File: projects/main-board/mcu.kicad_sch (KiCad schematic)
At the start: 106 parts, among them J4 TC2030, J7 Conn_01x06, U1 STM32N657X0HxQ

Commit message: Updated schematics with new symbols
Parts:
- removed U1: STM32N657X0HxQ, VFBGA264, symbol stm32n_u:STM32N657X0HxQ
- added U15: STM32N657X0HxQ, footprint-library:STM32N645A0HxQ, symbol symbol-library:STM32N657X0HxQ
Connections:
- net 1V8: now also U15.G13 (VDD), U15.H12 (VDD), U15.H13 (VDD), U15.J12 (VDD), U15.J13 (VDD), U15.K13 (VDD)
- net BACKLIGHT_PWM: now also U15.B9 (PC6)
- net BOOT0: now also U15.G4 (BOOT0)
- net BUTTONS.B0: now also U15.R3 (PF0)
- net BUTTONS.B1: now also U15.P4 (PF1)
- net BUTTONS.B10: now also U15.L4 (PF10)
- net BUTTONS.B11: now also U15.P3 (PF11)
- net BUTTONS.B12: now also U15.T1 (PF12)
- net BUTTONS.B13: now also U15.R2 (PF13)
- net BUTTONS.B14: now also U15.N2 (PF14)
- net BUTTONS.B15: now also U15.N1 (PF15)
- net BUTTONS.B2: now also U15.N4 (PF2)
- net BUTTONS.B3: now also U15.M2 (PF3)
- net BUTTONS.B4: now also U15.L2 (PF4)
- net BUTTONS.B5: now also U15.M3 (PF5)
- net BUTTONS.B6: now also U15.L5 (PF6)
- net BUTTONS.B7: now also U15.M1 (PF7)
- net BUTTONS.B8: now also U15.N3 (PF8)
- net BUTTONS.B9: now also U15.P1 (PF9)
- net DEBUG_UART.RX: now also U15.R7 (PA10)
- net DEBUG_UART.TX: now also U15.P7 (PA9)
- net ESP32_EN: now also U15.F13 (PB3)
- net ESP32_GPIO.2: now also U15.C8 (PC12)
- net ESP32_GPIO.3: now also U15.A9 (PC1)
- net ESP32_GPIO.8: now also U15.F3 (PC13)
- net ESP32_GPIO.9: now also U15.A8 (PC10)
- net ESP32_UART.RX: now also U15.F17 (PE1)
- net ESP32_UART.TX: now also U15.F16 (PE0)
- net FLASH_OCTOSPI.RESET_N: now also U15.T16 (PN7)
- net GND: now also U15.A17 (VSS), U15.F10 (VSS), U15.F11 (VSS), U15.F12 (VSS), U15.F2 (VSSAPMU), U15.F7 (VSS), U15.G12 (VSS), U15.G6 (VSSAON), U15.H1 (VSSSMPS), U15.H2 (VSSSMPS), U15.H3 (VSSSMPS), U15.H4 (VSSSMPS), U15.H5 (VSSSMPS), U15.H6 (VSSSMPS), U15.K12 (VSS), U15.M10 (VSS), U15.M12 (VSS), U15.M13 (VSS), U15.M6 (VSSA), U15.M8 (VSS), U15.N11 (VSS), U15.N5 (VSS), U15.N7 (VSS), U15.N9 (VSS), U15.T2 (VREF-), U15.U1 (VSS), U15.U17 (VSS)
- net I2C1.SCL: now also U15.C11 (PE5)
- net I2C1.SDA: now also U15.D11 (PE6)
- net I2C4.SCL: now also U15.A11 (PE13)
- net I2C4.SDA: now also U15.B11 (PE14)
- net I2S.BCK: now also U15.E17 (PB6)
- net I2S.DACDAT: now also U15.E16 (PB7)
- net I2S.LRCK: now also U15.E15 (PB0)
- net I2S.MCLK: now also U15.F15 (PE2)
- net LCD.B0: now also U15.R6 (PG15)
- net LCD.B1: now also U15.R12 (PA7)
- net LCD.B2: now also U15.C16 (PB2)
- net LCD.B3: now also U15.L3 (PG6)
- net LCD.B4: now also U15.B1 (PH3)
- net LCD.B5: now also U15.B2 (PH6)
- net LCD.B6: now also U15.U8 (PA8)
- net LCD.B7: now also U15.T8 (PA2)
- net LCD.CLK: now also U15.C15 (PB13)
- net LCD.DE: now also U15.U9 (PG13)
- net LCD.EN: now also U15.D3 (PQ3)
- net LCD.G0: now also U15.T9 (PG12)
- net LCD.G1: now also U15.R9 (PG1)
- net LCD.G2: now also U15.P9 (PA1)
- net LCD.G3: now also U15.U10 (PA0)
- net LCD.G4: now also U15.D17 (PB15)
- net LCD.G5: now also U15.R10 (PB12)
- net LCD.G6: now also U15.P10 (PB11)
- net LCD.G7: now also U15.T14 (PG8)
- net LCD.HSYNC: now also U15.B17 (PB14)
- net LCD.R0: now also U15.R13 (PG0)
- net LCD.R1: now also U15.H14 (PD9)
- net LCD.R2: now also U15.B14 (PD15)
- net LCD.R3: now also U15.T12 (PB4(NJTRST))
- net LCD.R4: now also U15.F4 (PH4)
- net LCD.R5: now also U15.P12 (PA15(JTDI))
- net LCD.R6: now also U15.U13 (PG11)
- net LCD.R7: now also U15.E14 (PD8)
- net LCD.VSYNC: now also U15.E11 (PE11)
- net LEFT_MOTOR_PWM: now also U15.R8 (PA5)
- net NRST: now also U15.G3 (NRST)
- net PMIC_ALERT: now also U15.D13 (PD0)
- net PMIC_CHARGE_EN: now also U15.E13 (PD3)
- net PMIC_INPUT_VALID: now also U15.C12 (PD2)
- net PMIC_STATUS: now also U15.A14 (PD1)
- net RIGHT_MOTOR_PWM: now also U15.P8 (PA6)
- net SD.CLK: now also U15.D9 (PC2)
- net SD.CMD: now also U15.E10 (PC3)
- net SD.D0: now also U15.A10 (PC4)
- net SD.D1: now also U15.B10 (PC5)
- net SD.D2: now also U15.C10 (PC0)
- net SD.D3: now also U15.D10 (PE4)
- net SD.DETECT: now also U15.P14 (PN12)
- net SWCLK: now also U15.T6 (PA14(JTCK/SWCLK))
- net SWDIO: now also U15.U6 (PA13(JTMS/SWDIO))
- net USB.DM: now also U15.A5 (OTG1_HSDM)
- net USB.DP: now also U15.B5 (OTG1_HSDP)
- net USB_CC1: now also U15.A6 (UCPD1_CC1)
- net USB_CC2: now also U15.B6 (UCPD1_CC2)
- net V08CAP: now also U15.F1 (V08CAP)
- net VDDA18ADC: now also U15.N6 (VDDA18ADC)
- net VDDA18AON: now also U15.A1 (PDR_ON), U15.F6 (VDDA18AON)
- net VDDA18CSI: now also U15.R5 (VDDA18CSI)
- net VDDA18PLL: now also U15.M5 (VDDA18PLL)
- net VDDA18PMU: now also U15.G1 (VDDA18PMU)
- net VDDA18USB: now also U15.C5 (VDDA18USB)
- net VDDA33USB: now also U15.A4 (VDD33USB)
- net VDDCORE: now also U15.G2 (VFBSMPS), U15.L12 (VDDCORE), U15.L6 (VDDCORE), U15.M11 (VDDCORE), U15.M7 (VDDCORE), U15.M9 (VDDCORE), U15.N10 (VDDCORE), U15.N12 (VDDCORE), U15.N8 (VDDCORE), U15.P11 (VDDCORE)
- net VDDCSI: now also U15.R4 (VDDCSI)
- net VDDIO2: now also U15.L13 (VDDIO2), U15.L14 (VDDIO2), U15.M14 (VDDIO2), U15.M15 (VDDIO2)
- net VDDIO3: now also U15.N13 (VDDIO3), U15.P13 (VDDIO3)
- net VDDIO4: now also U15.E8 (VDDIO4), U15.F8 (VDDIO4)
- net VDDIO5: now also U15.E9 (VDDIO5), U15.F9 (VDDIO5)
- net VDDSMPS: now also U15.K1 (VDDSMPS), U15.K2 (VDDSMPS), U15.K3 (VDDSMPS), U15.K4 (VDDSMPS), U15.K5 (VDDSMPS), U15.K6 (VDDSMPS)
- net VREF: now also U15.U2 (VREF+)
- net at R46.1: now also U15.L17 (PP14)
- net at R40.1: now also U15.L16 (PP8)
- net at L1.1, R2.1: now also U15.J1 (VLXSMPS), U15.J2 (VLXSMPS), U15.J3 (VLXSMPS), U15.J4 (VLXSMPS), U15.J5 (VLXSMPS), U15.J6 (VLXSMPS)
- net at R36.1: now also U15.H15 (PP4)
- net at R58.2: now also U15.C6 (OTG1_TXRTUNE)
- net at R22.1: now also U15.N17 (PN4)
- net at R24.1: now also U15.P15 (PN6)
- net at R25.1: now also U15.P16 (PN8)
- net at R16.1: now also U15.P17 (PN0)
- net at R21.1: now also U15.R15 (PN3)
- net at R23.1: now also U15.R16 (PN5)
- net at R19.1: now also U15.R17 (PN1)
- net at R26.1: now also U15.T15 (PN9)
- net at R20.1: now also U15.T17 (PN2)
- net at R27.1: now also U15.U15 (PN10)
- net at R28.1: now also U15.U16 (PN11)
- net at R56.1, R57.2: now also U15.E1 (VBAT)
- net at R29.1: now also U15.K17 (PO2)
- net at R43.1: now also U15.L15 (PP11)
- net at R31.1: now also U15.N16 (PO4)
- net at R32.1: now also U15.G17 (PP0)
- net at R44.1: now also U15.J15 (PP12)
- net at R30.1: now also U15.M16 (PO3)
- net at R15.1: now also U15.M17 (PO0)
- net at R47.1: now also U15.H17 (PP15)
- net at R41.1: now also U15.N14 (PP9)
- net at R42.1: now also U15.N15 (PP10)
- net at R35.1: now also U15.J16 (PP3)
- net at R33.1: now also U15.H16 (PP1)
- net at R37.1: now also U15.J14 (PP5)
- net at R38.1: now also U15.G16 (PP6)
- net at R39.1: now also U15.G15 (PP7)
- net at R34.1: now also U15.J17 (PP2)
- net at R45.1: now also U15.K14 (PP13)

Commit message: Re-annotate schematics.
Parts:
- renumbered C2 to C1, C21 to C10, C1 to C11, C37 to C12, C35 to C13, C47 to C14, C9 to C15, C15 to C16, C42 to C17, C22 to C18, C3 to C19, C19 to C2, C38 to C20, C48 to C21, C33 to C22, C10 to C24, C43 to C25, C16 to C26, C4 to C27, C39 to C28, C20 to C29, C30 to C3, C31 to C30, C24 to C31, C11 to C32, C44 to C33, C17 to C34, C5 to C35, C40 to C36, C18 to C37, C25 to C38, C29 to C39, C36 to C4, C45 to C40, C6 to C41, C12 to C42, C32 to C43, C26 to C44, C46 to C45, C13 to C46, C27 to C47, C28 to C48, C34 to C5, C7 to C6, C8 to C7, C14 to C8, C41 to C9, J4 to J1, J7 to J2, L3 to L2, NT12 to NT1, NT1 to NT10, NT7 to NT11, NT10 to NT12, NT3 to NT13, NT8 to NT14, NT9 to NT2, NT13 to NT3, NT2 to NT4, NT4 to NT5, NT14 to NT7, NT11 to NT8, NT5 to NT9, R2 to R1, R19 to R10, R20 to R11, R21 to R12, R22 to R13, R23 to R14, R24 to R15, R25 to R16, R26 to R17, R27 to R18, R28 to R19, R58 to R2, R15 to R20, R29 to R21, R30 to R22, R31 to R23, R32 to R24, R33 to R25, R34 to R26, R35 to R27, R36 to R28, R37 to R29, R56 to R3, R38 to R30, R39 to R31, R40 to R32, R41 to R33, R42 to R34, R43 to R35, R44 to R36, R45 to R37, R46 to R38, R47 to R39, R57 to R4, R54 to R5, R52 to R6, R55 to R7, R53 to R8, R16 to R9, U15 to U1

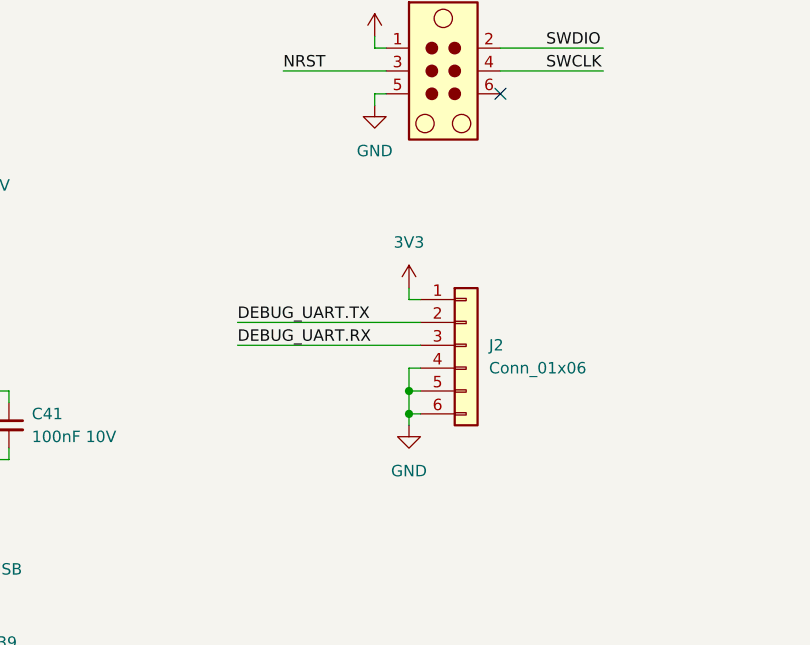
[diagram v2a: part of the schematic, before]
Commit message: Replace 0.1in header with TC2030
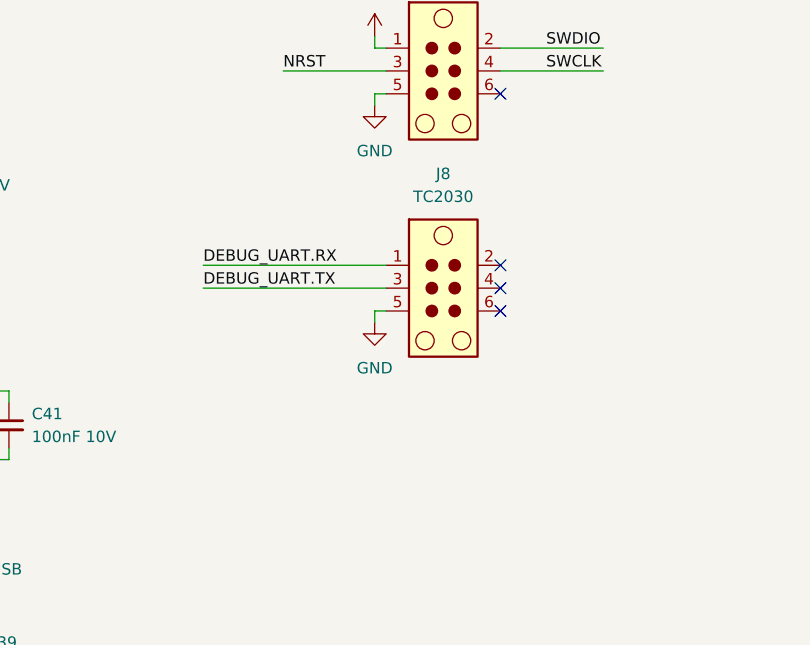
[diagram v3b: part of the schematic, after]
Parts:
- removed J2: Conn_01x06, symbol Connector_Generic:Conn_01x06
- added J8: TC2030, Connector:Tag-Connect_TC2030-IDC-NL_2x03_P1.27mm_Vertical, symbol Connector:TC2030
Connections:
- net DEBUG_UART.RX: now also J8.1
- net DEBUG_UART.TX: now also J8.3
- net GND: now also J8.5
- no-connect marks 14 -> 17

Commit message: Add capacitor part library.
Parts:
- C10, C18, C2, C21, C23, C25, C31, C33, C37, C38, C39, C44, C47, C48: value 1uF 6.3V -> 1uF 10V
- C12, C20, C28, C36: value 22uF 6.3V -> 22uF 10V
- C17, C9: value 10uF 6.3V -> 10uF 10V
- C3: value 2.2nF 6.3V -> 2.2nF 10V
- C4: value 4.7uF 6.3V -> 4.7uF 10V
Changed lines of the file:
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@@
 			)
 		)
-		(property "Value" "22uF 6.3V"
+		(property "Value" "22uF 10V"
 			(at 146.05 120.6562 0)
 			(effects
@@
 			)
 		)
-		(property "Value" "10uF 6.3V"
+		(property "Value" "10uF 10V"
 			(at 110.49 359.4162 0)
 			(effects
@@
 			)
 		)
-		(property "Value" "1uF 6.3V"
+		(property "Value" "1uF 10V"
 			(at 201.93 248.9262 0)
 			(effects
@@
 			)
 		)
-		(property "Value" "2.2nF 6.3V"
+		(property "Value" "2.2nF 10V"
 			(at 110.236 120.396 90)
 			(effects
@@
 			)
 		)
-		(property "Value" "1uF 6.3V"
+		(property "Value" "1uF 10V"
 			(at 152.4 359.4162 0)
 			(effects
@@
 			)
 		)
-		(property "Value" "22uF 6.3V"
+		(property "Value" "22uF 10V"
 			(at 160.02 120.6562 0)
 			(effects
@@
 			)
 		)
-		(property "Value" "1uF 6.3V"
+		(property "Value" "1uF 10V"
 			(at 113.03 248.9262 0)
 			(effects
@@
 			)
 		)
-		(property "Value" "1uF 6.3V"
+		(property "Value" "1uF 10V"
 			(at 163.83 248.9262 0)
 			(effects
@@
 			)
 		)
-		(property "Value" "1uF 6.3V"
+		(property "Value" "1uF 10V"
 			(at 165.1 199.3962 0)
 			(effects
@@
 			)
 		)
-		(property "Value" "10uF 6.3V"
+		(property "Value" "10uF 10V"
 			(at 124.46 359.4162 0)
 			(effects
@@
 			)
 		)
-		(property "Value" "1uF 6.3V"
+		(property "Value" "1uF 10V"
 			(at 151.13 248.9262 0)
 			(effects
@@
 			)
 		)
-		(property "Value" "1uF 6.3V"
+		(property "Value" "1uF 10V"
 			(at 138.43 248.9262 0)
 			(effects
@@
 			)
 		)
-		(property "Value" "1uF 6.3V"
+		(property "Value" "1uF 10V"
 			(at 125.73 248.9262 0)
 			(effects
@@
 			)
 		)
-		(property "Value" "22uF 6.3V"
+		(property "Value" "22uF 10V"
 			(at 132.08 120.6562 0)
 			(effects
@@
 			)
 		)
-		(property "Value" "1uF 6.3V"
+		(property "Value" "1uF 10V"
 			(at 160.02 146.0562 0)
 			(effects
@@
 			)
 		)
-		(property "Value" "1uF 6.3V"
+		(property "Value" "1uF 10V"
 			(at 134.62 273.0562 0)
 			(effects
@@
 			)
 		)
-		(property "Value" "1uF 6.3V"
+		(property "Value" "1uF 10V"
 			(at 100.33 248.9262 0)
 			(effects
@@
 			)
 		)
-		(property "Value" "4.7uF 6.3V"
+		(property "Value" "4.7uF 10V"
 			(at 104.14 146.0562 0)
 			(effects
@@
 			)
 		)
-		(property "Value" "1uF 6.3V"
+		(property "Value" "1uF 10V"
 			(at 176.53 248.9262 0)
 			(effects
@@
 			)
 		)
-		(property "Value" "1uF 6.3V"
+		(property "Value" "1uF 10V"
 			(at 138.43 359.4162 0)
 			(effects
@@
 			)
 		)
-		(property "Value" "22uF 6.3V"
+		(property "Value" "22uF 10V"
 			(at 118.11 120.6562 0)
 			(effects
@@
 			)
 		)
-		(property "Value" "1uF 6.3V"
+		(property "Value" "1uF 10V"
 			(at 189.23 248.9262 0)
 			(effects

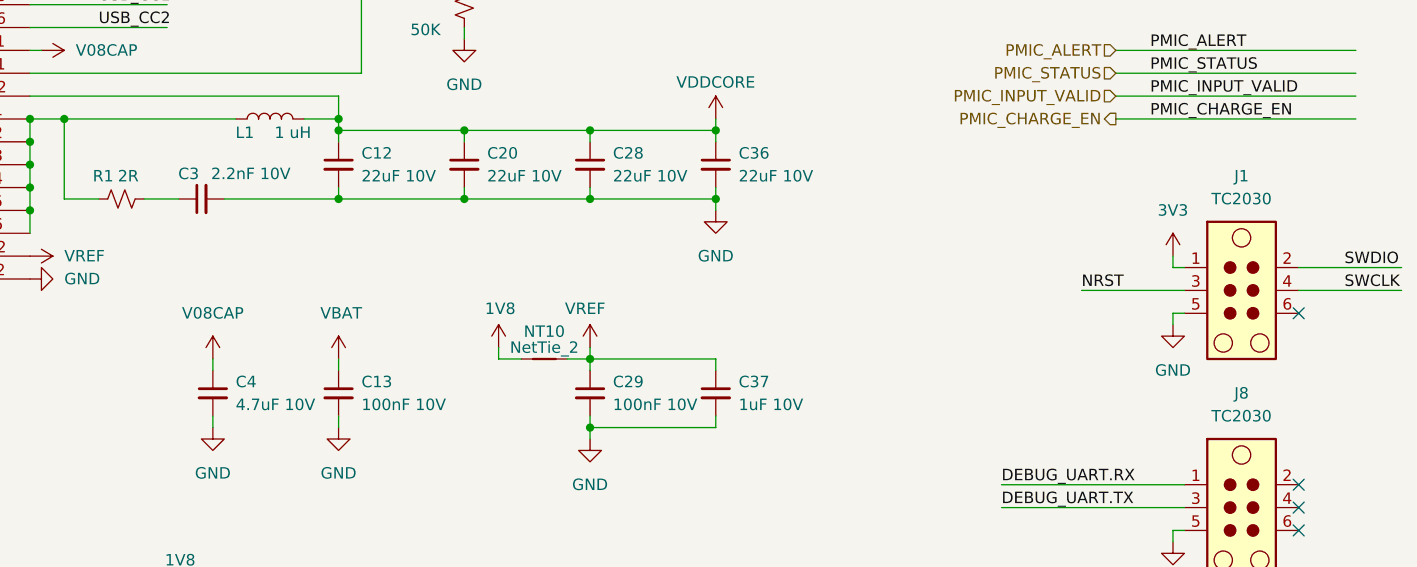
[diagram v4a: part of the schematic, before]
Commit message: Normalise capacitors
- Add capacitor parts to library.
- Replace all placeholder capacitors
  with the actual part numbers.
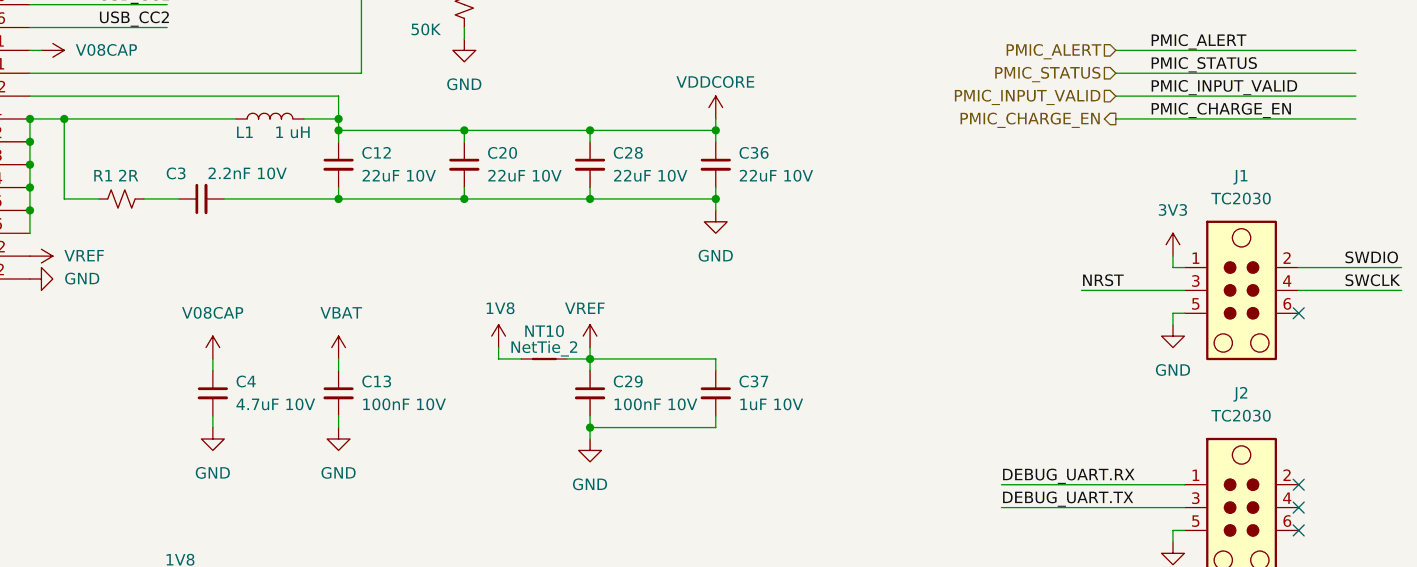
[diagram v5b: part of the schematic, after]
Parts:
- removed C1, C11, C13, C14, C15, C16, C19, C22, C24, C26, C27, C29, C30, C32, C34, C35, C40, C41, C42, C43, C45, C46, C5, C6, C7, C8: 100nF 10V, symbol Device:C_Small
- removed C10, C18, C2, C21, C23, C25, C31, C33, C37, C38, C39, C44, C47, C48: 1uF 10V, symbol Device:C_Small
- removed C12, C20, C28, C36: 22uF 10V, symbol Device:C_Small
- removed C17, C9: 10uF 10V, symbol Device:C_Small
- removed C3: 2.2nF 10V, symbol Device:C_Small
- removed C4: 4.7uF 10V, symbol Device:C_Small
- added C1, C11, C13, C14, C15, C16, C19, C22, C24, C26, C27, C29, C30, C32, C34, C35, C40, C41, C42, C43, C45, C46, C5, C6, C7, C8: 100nF 10V, Capacitor_SMD:C_0402_1005Metric, symbol symbol-library-capacitors:CC0402KRX7R6BB104
- added C10, C18, C2, C21, C23, C25, C31, C33, C37, C38, C39, C44, C47, C48: 1uF 10V, Capacitor_SMD:C_0402_1005Metric, symbol symbol-library-capacitors:CC0402KRX5R6BB105
- added C12, C20, C28, C36: 22uF 10V, Capacitor_SMD:C_0603_1608Metric, symbol symbol-library-capacitors:CC0603MPX5R6BB226
- added C17, C9: 10uF 10V, Capacitor_SMD:C_0603_1608Metric, symbol symbol-library-capacitors:CC0603MRX5R6BB106
- added C3: 2.2nF 10V, Capacitor_SMD:C_0402_1005Metric, symbol symbol-library-capacitors:CC0402KRX7R6BB222
- added C4: 4.7uF 10V, Capacitor_SMD:C_0402_1005Metric, symbol symbol-library-capacitors:CC0402MRX5R6BB475
- renumbered J8 to J2
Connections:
- net 1V8: now also C1.1, C11.1, C19.1, C27.1, C35.1, C41.1
- net GND: now also C1.2, C10.2, C11.2, C12.2, C13.2, C14.2, C15.2, C16.2, C17.2, C18.2, C19.2, C2.2, C20.2, C21.2, C22.2, C23.2, C24.2, C25.2, C26.2, C27.2, C28.2, C29.2, C3.2, C30.2, C31.2, C32.2, C33.2, C34.2, C35.2, C36.2, C37.2, C38.2, C39.2, C4.2, C40.2, C41.2, C42.2, C43.2, C44.2, C45.2, C46.2, C47.2, C48.2, C5.2, C6.2, C7.2, C8.2, C9.2
- net V08CAP: now also C4.1
- net VBAT: now also C13.1
- net VDDA18ADC: now also C30.1
- net VDDA18AON: now also C5.1
- net VDDA18CSI: now also C6.1
- net VDDA18PLL: now also C43.1
- net VDDA18USB: now also C22.1
- net VDDA33USB: now also C39.1
- net VDDCORE: now also C10.1, C12.1, C18.1, C2.1, C20.1, C23.1, C28.1, C31.1, C36.1, C38.1, C44.1, C47.1, C48.1
- net VDDCSI: now also C21.1
- net VDDIO2: now also C15.1, C24.1, C32.1, C7.1
- net VDDIO3: now also C42.1, C46.1
- net VDDIO4: now also C16.1, C8.1
- net VDDIO5: now also C26.1, C34.1
- net VDDSMPS: now also C17.1, C25.1, C33.1, C40.1, C45.1, C9.1
- net VREF: now also C29.1, C37.1
- net at R1.2: now also C3.1
- net at L2.1: now also C14.1

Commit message: Replace placeholder resistors
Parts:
- removed R1: 2R, symbol Device:R_Small_US
- removed R10, R11, R12, R13, R14, R15, R16, R17, R18, R19, R20, R21, R22, R23, R24, R25, R26, R27, R28, R29, R30, R31, R32, R33, R34, R35, R36, R37, R38, R39, R9: 0R, symbol Device:R_Small_US
- removed R2: 200R, symbol Device:R_Small_US
- removed R3: 10K, symbol Device:R_Small_US
- removed R4: 50K, symbol Device:R_Small_US
- removed R5, R6, R7, R8: 2.2K, symbol Device:R_Small_US
- added R1, R10, R11, R12, R13, R14, R15, R16, R17, R18, R19, R2, R20, R21, R22, R23, R24, R25, R26, R27, R28, R29, R3, R30, R31, R32, R33, R34, R35, R4, R9: 0R, Resistor_SMD:R_0402_1005Metric, symbol symbol-library-resistors:RC0402FR-070RL
- added R5, R6, R61, R7: 2.2K, Resistor_SMD:R_0402_1005Metric, symbol symbol-library-resistors:RC0402JR-072K2L
- added R62: 10K, Resistor_SMD:R_0402_1005Metric, symbol symbol-library-resistors:RC0402JR-0710KL
- added R63: 200R, Resistor_SMD:R_0402_1005Metric, symbol symbol-library-resistors:RC0402FR-07200RL
- added R64: 2R, Resistor_SMD:R_0402_1005Metric, symbol symbol-library-resistors:RC0402FR-072RL
- added R8: 50.1K, Resistor_SMD:R_0402_1005Metric, symbol symbol-library-resistors:RT0402BRD0750K5L
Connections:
- net 3V3: now also R5.1, R6.1, R61.1, R7.1
- net FLASH_OCTOSPI.CS_N: now also R2.2
- net FLASH_OCTOSPI.DQS: now also R1.2
- net FLASH_OCTOSPI.SCLK: now also R11.2
- net FLASH_OCTOSPI.SIO0: now also R3.2
- net FLASH_OCTOSPI.SIO1: now also R4.2
- net FLASH_OCTOSPI.SIO2: now also R9.2
- net FLASH_OCTOSPI.SIO3: now also R10.2
- net FLASH_OCTOSPI.SIO4: now also R12.2
- net FLASH_OCTOSPI.SIO5: now also R13.2
- net FLASH_OCTOSPI.SIO6: now also R14.2
- net FLASH_OCTOSPI.SIO7: now also R15.2
- net GND: now also R63.2, R8.2
- net I2C1.SCL: now also R7.2
- net I2C1.SDA: now also R6.2
- net I2C4.SCL: now also R61.2
- net I2C4.SDA: now also R5.2
- net RAM_HEXASPI.CLK: now also R19.2
- net RAM_HEXASPI.CS_N: now also R16.2
- net RAM_HEXASPI.D0: now also R20.2
- net RAM_HEXASPI.D1: now also R21.2
- net RAM_HEXASPI.D10: now also R30.2
- net RAM_HEXASPI.D11: now also R31.2
- net RAM_HEXASPI.D12: now also R32.2
- net RAM_HEXASPI.D13: now also R33.2
- net RAM_HEXASPI.D14: now also R34.2
- net RAM_HEXASPI.D15: now also R35.2
- net RAM_HEXASPI.D2: now also R22.2
- net RAM_HEXASPI.D3: now also R23.2
- net RAM_HEXASPI.D4: now also R24.2
- net RAM_HEXASPI.D5: now also R25.2
- net RAM_HEXASPI.D6: now also R26.2
- net RAM_HEXASPI.D7: now also R27.2
- net RAM_HEXASPI.D8: now also R28.2
- net RAM_HEXASPI.D9: now also R29.2
- net RAM_HEXASPI.DQS0: now also R17.2
- net RAM_HEXASPI.DQS1: now also R18.2
- net VBAT: now also R62.1
- net at U1.L17 (PP14): now also R34.1
- net at C3.1: now also R64.2
- net at U1.L16 (PP8): now also R28.1
- net at L1.1, U1.J1 (VLXSMPS), U1.J2 (VLXSMPS)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: now also R64.1
- net at U1.H15 (PP4): now also R24.1
- net at U1.C6 (OTG1_TXRTUNE): now also R63.1
- net at U1.K17 (PO2): now also R17.1
- net at U1.P15 (PN6): now also R11.1
- net at U1.L15 (PP11): now also R31.1
- net at U1.N16 (PO4): now also R19.1
- net at U1.G17 (PP0): now also R20.1
- net at U1.J15 (PP12): now also R32.1
- net at U1.E1 (VBAT): now also R62.2, R8.1
- net at U1.R17 (PN1): now also R2.1
- net at U1.N17 (PN4): now also R9.1
- net at U1.P16 (PN8): now also R12.1
- net at U1.P17 (PN0): now also R1.1
- net at U1.R15 (PN3): now also R4.1
- net at U1.R16 (PN5): now also R10.1
- net at U1.T15 (PN9): now also R13.1
- net at U1.T17 (PN2): now also R3.1
- net at U1.U15 (PN10): now also R14.1
- net at U1.U16 (PN11): now also R15.1
- net at U1.H17 (PP15): now also R35.1
- net at U1.N14 (PP9): now also R29.1
- net at U1.M16 (PO3): now also R18.1
- net at U1.M17 (PO0): now also R16.1
- net at U1.N15 (PP10): now also R30.1
- net at U1.J16 (PP3): now also R23.1
- net at U1.H16 (PP1): now also R21.1
- net at U1.J14 (PP5): now also R25.1
- net at U1.G15 (PP7): now also R27.1
- net at U1.G16 (PP6): now also R26.1
- net at U1.J17 (PP2): now also R22.1
- net at U1.K14 (PP13): now also R33.1

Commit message: Add footprints
- Inductors
- Switches
- Buttons
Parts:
- removed L1: 1 uH, symbol Device:L
- removed L2: 0.9 nH, symbol Device:L
- added L1: 1uH 2.7A 0.054R, footprint-library:IND_0806, symbol symbol-library-inductors:DFE201612P-1R0M=P2
- added L2: 18R, Inductor_SMD:L_0603_1608Metric, symbol symbol-library-inductors:LSMCA160808T180NGR
- added L3: 2.2nH 1.4A 0.018R, Inductor_SMD:L_0603_1608Metric, symbol symbol-library-inductors:LQW18AN2N2D10D
- renumbered C11 to C10, C12 to C11, C13 to C12, C14 to C13, C15 to C14, C16 to C15, C9 to C16, C18 to C17, C19 to C18, C20 to C19, C21 to C20, C22 to C21, C23 to C22, C24 to C23, C17 to C24, C26 to C25, C27 to C26, C28 to C27, C29 to C28, C30 to C29, C31 to C30, C32 to C31, C25 to C32, C34 to C33, C35 to C34, C36 to C35, C37 to C36, C38 to C37, C39 to C38, C33 to C39, C41 to C40, C42 to C41, C43 to C42, C44 to C43, C40 to C44, C46 to C45, C47 to C46, C45 to C47, C10 to C9, R64 to R1, R2 to R10, R3 to R11, R4 to R12, R9 to R13, R10 to R14, R11 to R15, R12 to R16, R13 to R17, R14 to R18, R15 to R19, R63 to R2, R16 to R20, R17 to R21, R18 to R22, R19 to R23, R20 to R24, R21 to R25, R22 to R26, R23 to R27, R24 to R28, R25 to R29, R62 to R3, R26 to R30, R27 to R31, R28 to R32, R29 to R33, R30 to R34, R31 to R35, R32 to R36, R33 to R37, R34 to R38, R35 to R39, R8 to R4, R7 to R5, R61 to R6, R6 to R7, R5 to R8, R1 to R9
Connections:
- net VDDA18PMU: now also L2.1
- net VDDCORE: now also L1.2
- net VDDSMPS: now also L3.1; no longer C16.1, C24.1, C32.1, C39.1, C44.1, C47.1
- net at C13.1: now also L2.2
- net at R1.1, U1.J1 (VLXSMPS), U1.J2 (VLXSMPS)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: now also L1.1
- new net: C16.1, C24.1, C32.1, C39.1, C44.1, C47.1, L3.2
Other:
- moved on the sheet: C16, C24, C32, C39, C44, C47
